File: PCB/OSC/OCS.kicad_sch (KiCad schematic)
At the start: 46 parts, among them J1 Reset, J2 Wago, J3 TC2030-USB-NL-DS, J4 SPK, J5 USB-C-Socket-H, J6 RELAY, SW1 Button, U1 ICS43434_MEMS_Mic, U2 ESP32-S3-MINI-1, U2 MAX98357A, U3 Relay, U4 78L05, U5 IRM-H638T/TR2, U5 MD8942

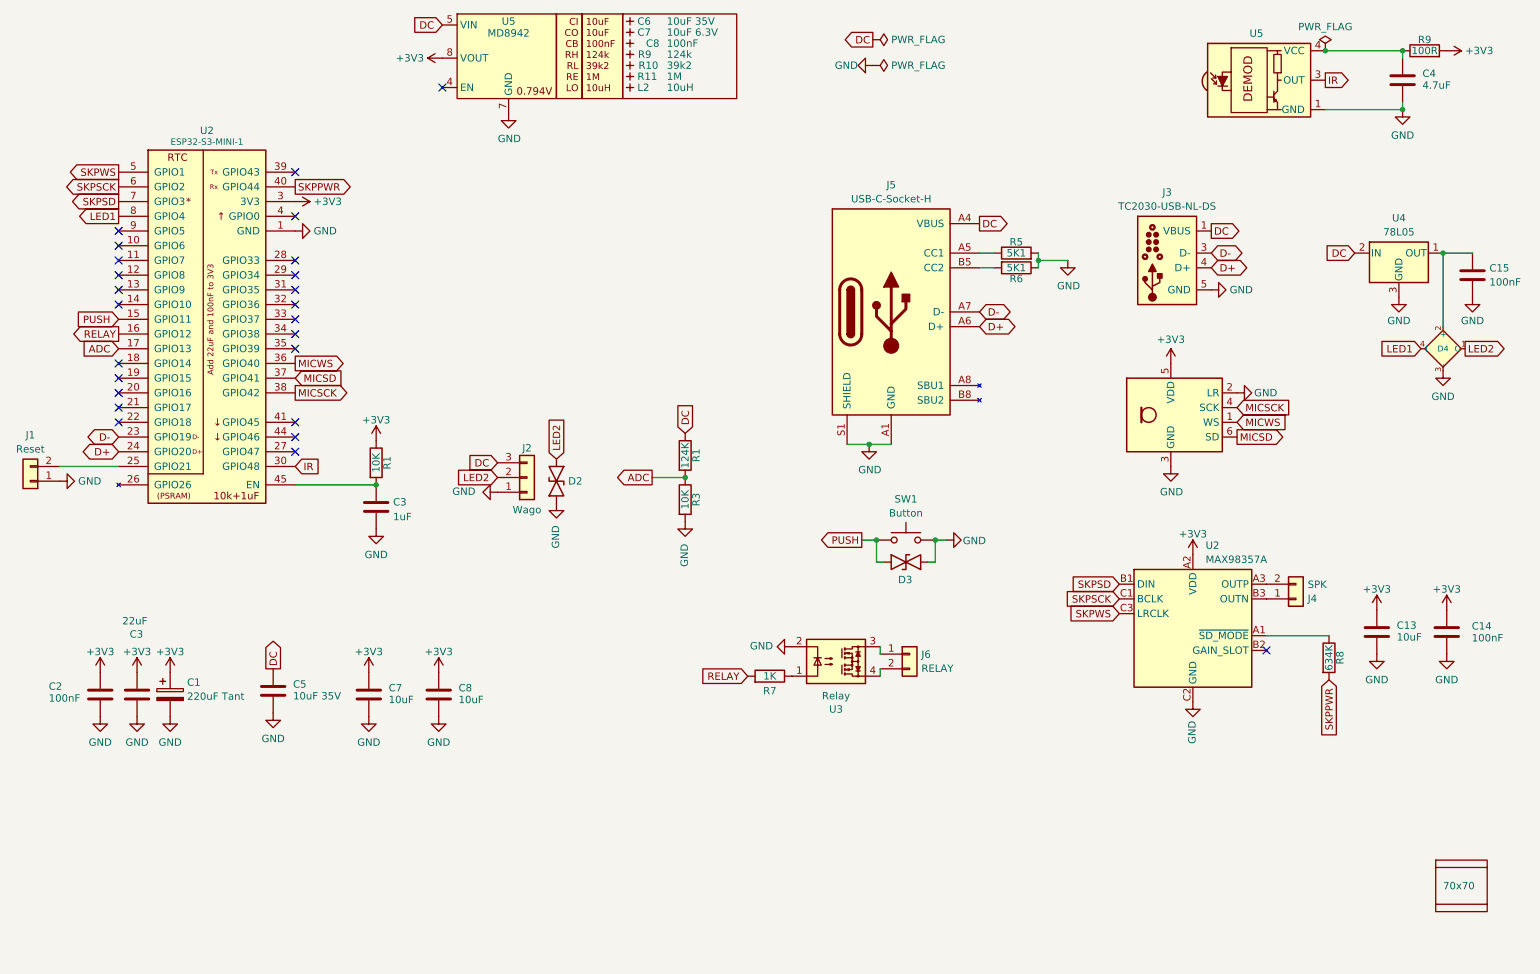
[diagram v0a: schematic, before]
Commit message: Getting basic BOM
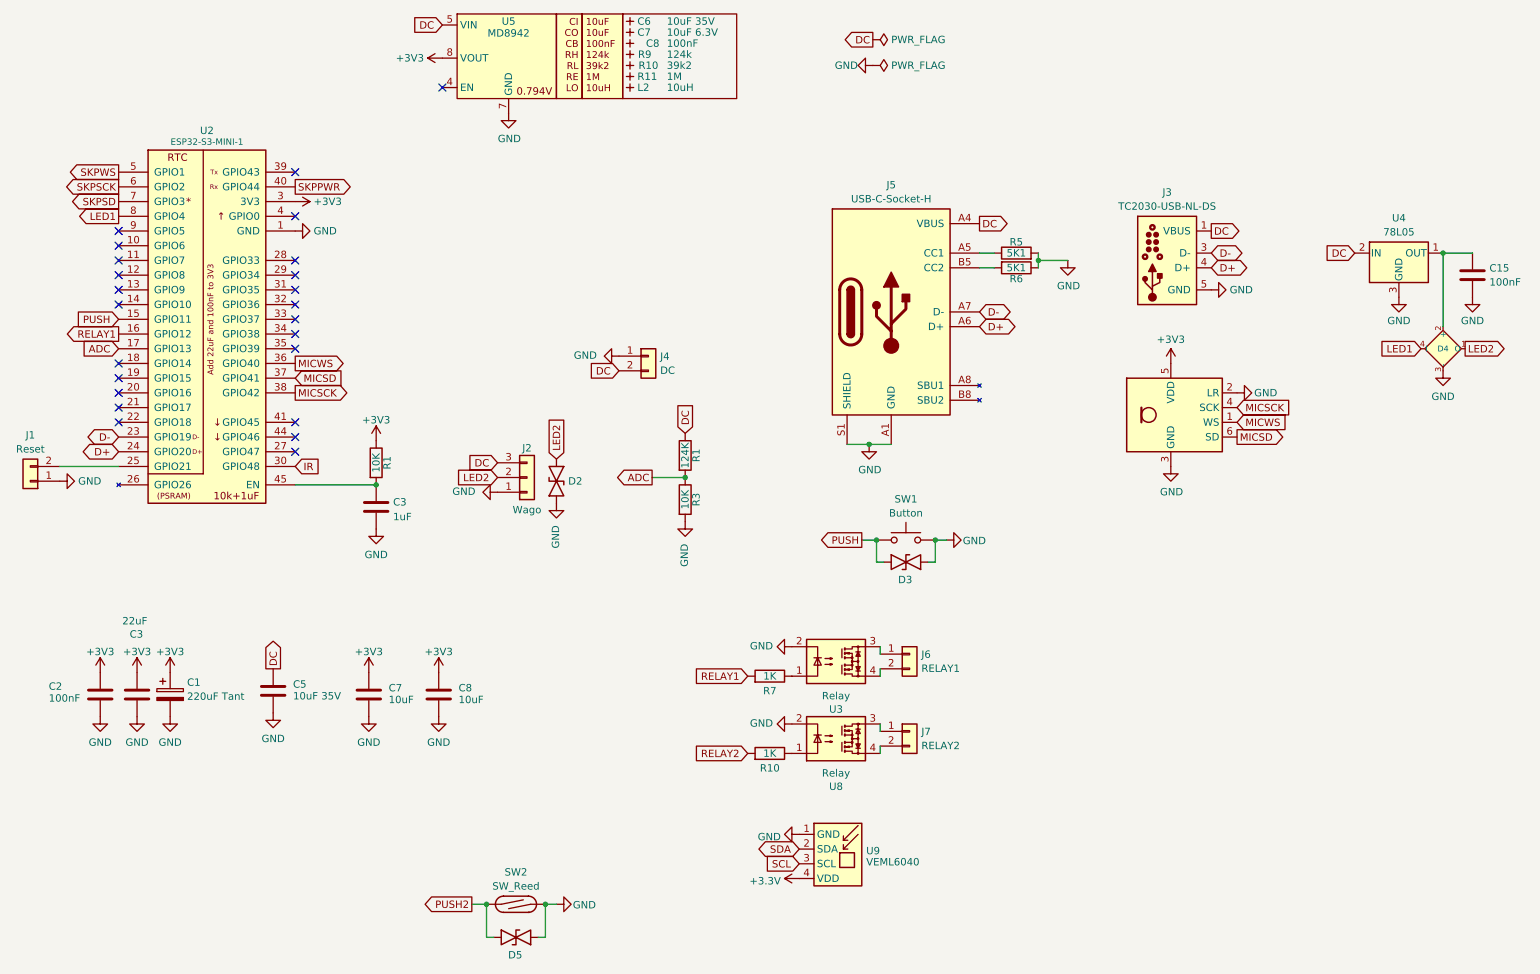
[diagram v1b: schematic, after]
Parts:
- removed C13: 10uF, RevK:C_0402, symbol Device:C
- removed C14: 100nF, RevK:C_0402, symbol Device:C
- removed C4: 4.7uF, RevK:C_0402, symbol Device:C
- removed PCB1: 70x70, RevK:PCB7070, symbol RevK:PCB
- removed R8: 634K, RevK:R_0402, symbol Device:R
- removed R9: 100R, RevK:R_0402, symbol Device:R
- removed U2: MAX98357A, RevK:WLP-1.437mmx1.347mm-0.21mm-ball, symbol RevK:MAX98357A
- removed U5: IRM-H638T/TR2, RevK:SMD-4P,4x5mm, symbol RevK:IRM-H638T/TR2
- removed V1, V2: ~, RevK:VCUT70N, symbol RevK:VCUT
- added D5: ~, RevK:DFN1006-2L, symbol RevK:ES05D1MC10
- added J7: RELAY2, RevK:WAGO-2060-452-998-404, symbol Connector_Generic:Conn_01x02
- added R10: 1K, RevK:R_0402, symbol Device:R
- added SW2: SW_Reed, symbol Switch:SW_Reed
- added U8: Relay, RevK:SO-4_4.4x4.3mm_P2.54mm, symbol RevK:G3VM-41GR8
- added U9: VEML6040, RevK:VEML6040, symbol RevK:VEML6040
- J4: value SPK -> DC
- J6: value RELAY -> RELAY1
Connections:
- net DC: now also J4.2 (Pin_2)
- net GND: now also J4.1 (Pin_1), D5.1, SW2.2, U8.2, U9.1 (GND)
- net RELAY renamed RELAY1
- new net: R10.1, U8.1
- new net: J7.1 (Pin_1), U8.3
- new net: J7.2 (Pin_2), U8.4
- new net +3.3V: U9.4 (VDD)
- new net PUSH2: D5.2, SW2.1
- new net RELAY2: R10.2
- new net SCL: U9.3 (SCL)
- new net SDA: U9.2 (SDA)
- no-connect marks 25 -> 24
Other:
- title: LED driver -> OSC widget
